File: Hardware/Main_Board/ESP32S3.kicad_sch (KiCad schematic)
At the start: 2 parts, among them U1 ESP32-S3-DEVKITC-1U-N8R2

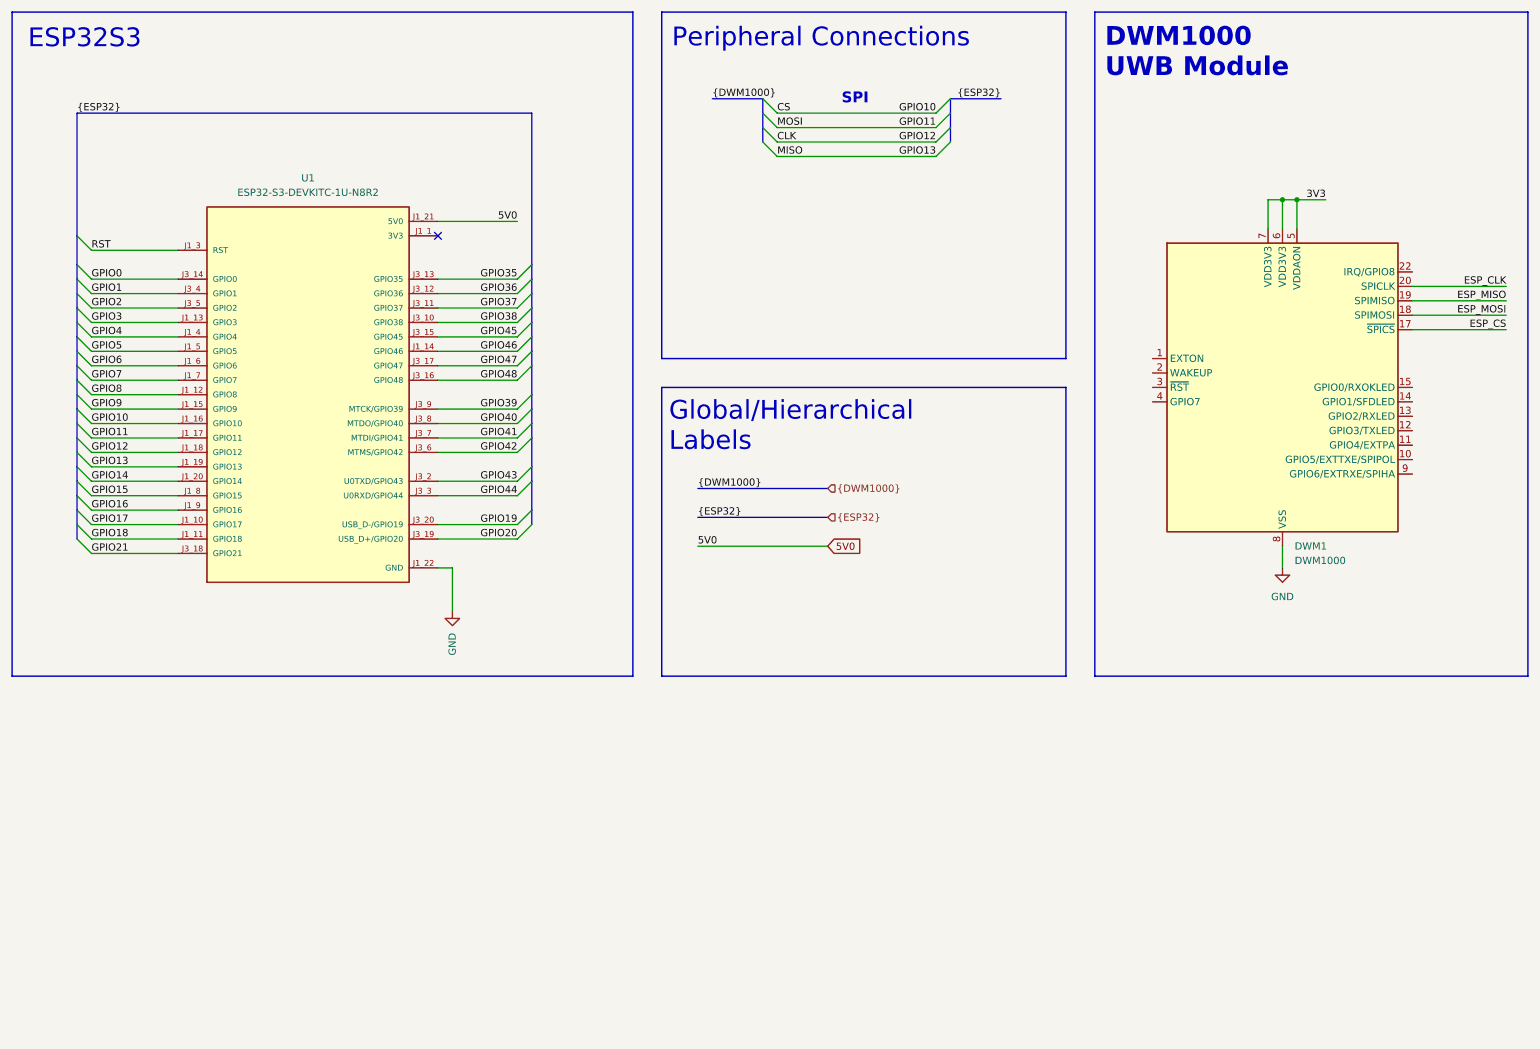
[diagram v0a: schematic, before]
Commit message: finished most of the main board
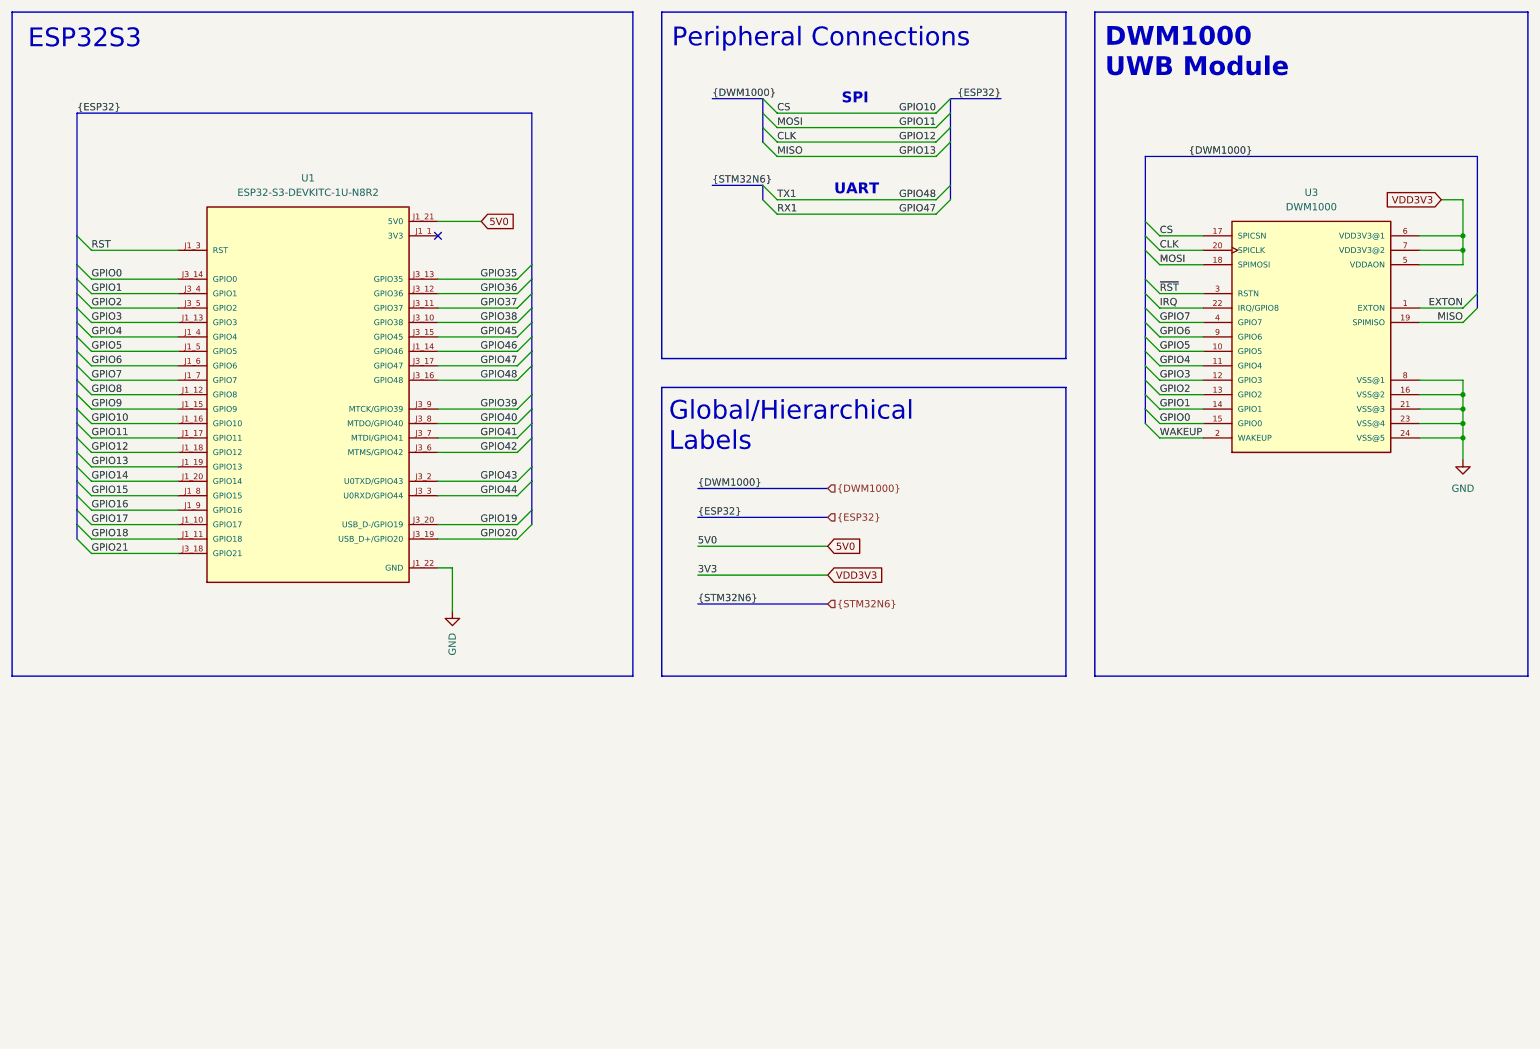
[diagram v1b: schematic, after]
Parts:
- removed DWM1: DWM1000, RF_Module:DWM1000, symbol RF_Module:DWM1000
- added U3: DWM1000, ESP32-footprints:BU01, symbol ESP32-Symbols:DWM1000
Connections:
- net 3V3: now also U3.5 (VDDAON), U3.6 (VDD3V3@1), U3.7 (VDD3V3@2)
- net CLK: now also U3.20 (SPICLK)
- net CS: now also U3.17 (SPICSN)
- net GND: now also U3.16 (VSS@2), U3.21 (VSS@3), U3.23 (VSS@4), U3.24 (VSS@5), U3.8 (VSS@1)
- net GPIO0: now also U3.15 (GPIO0)
- net GPIO1: now also U3.14 (GPIO1)
- net GPIO11: now also U3.18 (SPIMOSI)
- net GPIO13: now also U3.19 (SPIMISO)
- net GPIO2: now also U3.13 (GPIO2)
- net GPIO3: now also U3.12 (GPIO3)
- net GPIO4: now also U3.11 (GPIO4)
- net GPIO5: now also U3.10 (GPIO5)
- net GPIO6: now also U3.9 (GPIO6)
- net GPIO7: now also U3.4 (GPIO7)
- new net EXTON: U3.1 (EXTON)
- new net IRQ: U3.22 (IRQ/GPIO8)
- new net WAKEUP: U3.2 (WAKEUP)
- new net ~{RST}: U3.3 (RSTN)
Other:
- note added: "UART"

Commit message: added gerbers, drill files, BOM and CPL for the main board
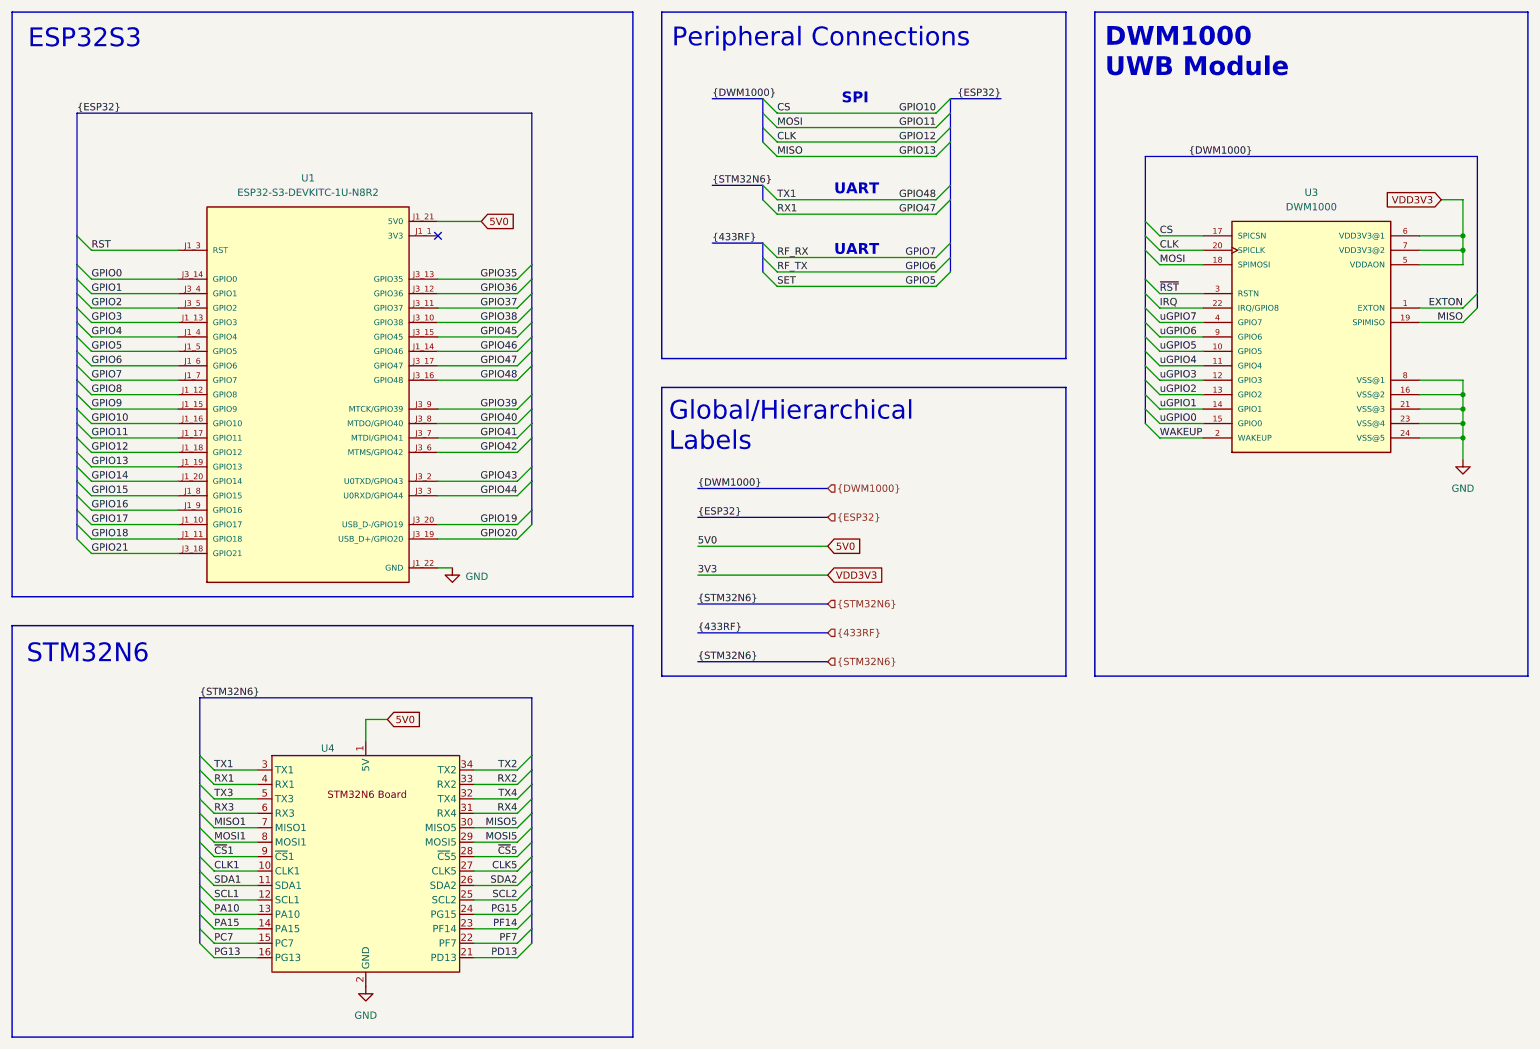
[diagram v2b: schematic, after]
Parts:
- added U4: ~, ESP32-footprints:STM32N6_Board, symbol ESP32-Symbols:STM32N6_Board
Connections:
- net GND: now also U4.18 (GND), U4.19 (GND), U4.2 (GND), U4.35 (GND), U4.GND1 (GND), U4.GND2 (GND), U4.GND3 (GND), U4.GND4 (GND)
- net GPIO0: no longer U3.15 (GPIO0)
- net GPIO1: no longer U3.14 (GPIO1)
- net GPIO2: no longer U3.13 (GPIO2)
- net GPIO3: no longer U3.12 (GPIO3)
- net GPIO4: no longer U3.11 (GPIO4)
- net GPIO47: now also U4.4 (RX1)
- net GPIO48: now also U4.3 (TX1)
- net GPIO5: no longer U3.10 (GPIO5)
- net GPIO6: no longer U3.9 (GPIO6)
- net GPIO7: no longer U3.4 (GPIO7)
- net 5V0 renamed 5V
- net 5V: now also U4.1 (5V), U4.17 (5V), U4.20 (5V), U4.36 (5V)
- new net CLK1: U4.10 (CLK1)
- new net CLK5: U4.27 (CLK5)
- new net MISO1: U4.7 (MISO1)
- new net MISO5: U4.30 (MISO5)
- new net MOSI1: U4.8 (MOSI1)
- new net MOSI5: U4.29 (MOSI5)
- new net PA10: U4.13 (PA10)
- new net PA15: U4.14 (PA15)
- new net PC7: U4.15 (PC7)
- new net PD13: U4.21 (PD13)
- new net PF14: U4.23 (PF14)
- new net PF7: U4.22 (PF7)
- new net PG13: U4.16 (PG13)
- new net PG15: U4.24 (PG15)
- new net RX2: U4.33 (RX2)
- new net RX3: U4.6 (RX3)
- new net RX4: U4.31 (RX4)
- new net SCL1: U4.12 (SCL1)
- new net SCL2: U4.25 (SCL2)
- new net SDA1: U4.11 (SDA1)
- new net SDA2: U4.26 (SDA2)
- new net TX2: U4.34 (TX2)
- new net TX3: U4.5 (TX3)
- new net TX4: U4.32 (TX4)
- new net uGPIO0: U3.15 (GPIO0)
- new net uGPIO1: U3.14 (GPIO1)
- new net uGPIO2: U3.13 (GPIO2)
- new net uGPIO3: U3.12 (GPIO3)
- new net uGPIO4: U3.11 (GPIO4)
- new net uGPIO5: U3.10 (GPIO5)
- new net uGPIO6: U3.9 (GPIO6)
- new net uGPIO7: U3.4 (GPIO7)
- new net ~{CS}1: U4.9 (~{CS}1)
- new net ~{CS}5: U4.28 (~{CS}5)
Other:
- note added: "STM32N6"
